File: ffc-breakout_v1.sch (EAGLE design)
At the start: 3 parts, among them X2 AMP_SFW16R-2STE1LF

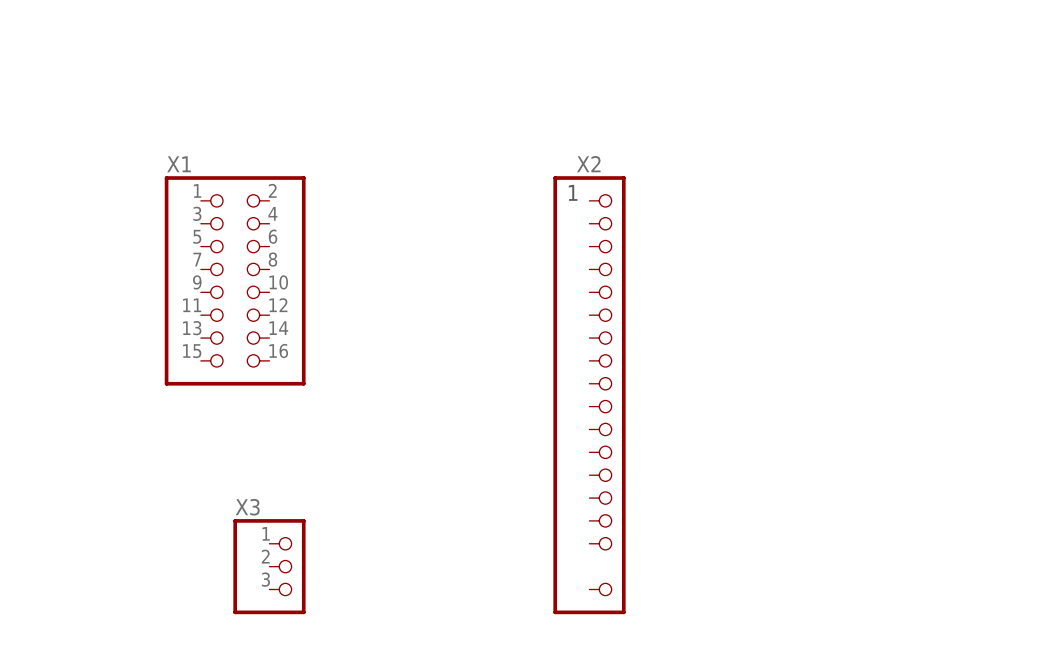
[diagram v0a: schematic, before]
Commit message: FFC breakout autoroute
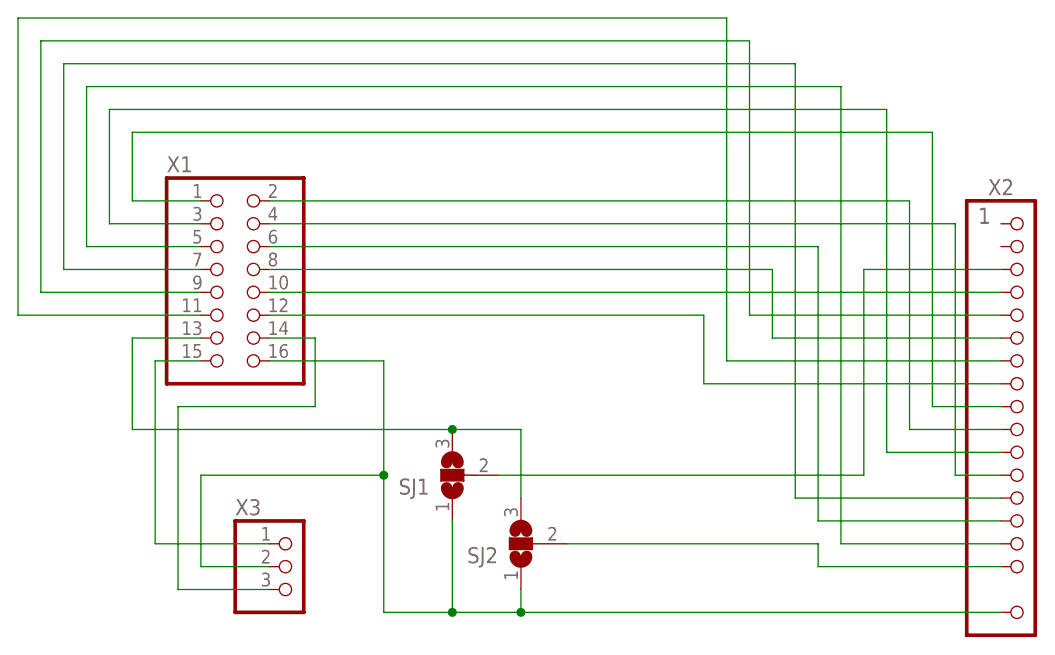
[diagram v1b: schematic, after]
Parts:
- added SJ1, SJ2: (no value), jumper:SJ2W
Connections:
- new net N$1: SJ1.1, SJ2.1, X1.16, X2.17, X3.2
- new net N$10: X1.4, X2.12
- new net N$11: X1.5, X2.15
- new net N$12: X1.6, X2.14
- new net N$13: X1.7, X2.13
- new net N$14: X1.8, X2.6
- new net N$15: X1.9, X2.5
- new net N$16: X1.10, X2.4
- new net N$17: X1.11, X2.7
- new net N$18: X1.12, X2.8
- new net N$2: X1.15, X3.1
- new net N$3: SJ1.3, SJ2.3, X1.13
- new net N$4: X1.14, X3.3
- new net N$5: SJ1.2, X2.3
- new net N$6: X1.1, X2.9
- new net N$7: SJ2.2, X2.16
- new net N$8: X1.2, X2.10
- new net N$9: X1.3, X2.11
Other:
- moved on the sheet: X2

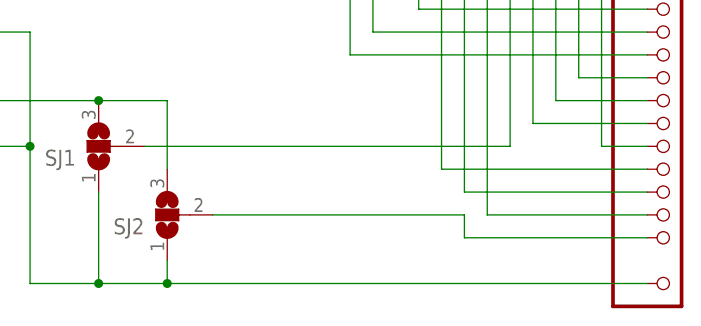
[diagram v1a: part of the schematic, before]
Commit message: FFC - much better autoroute + cleanup and markup
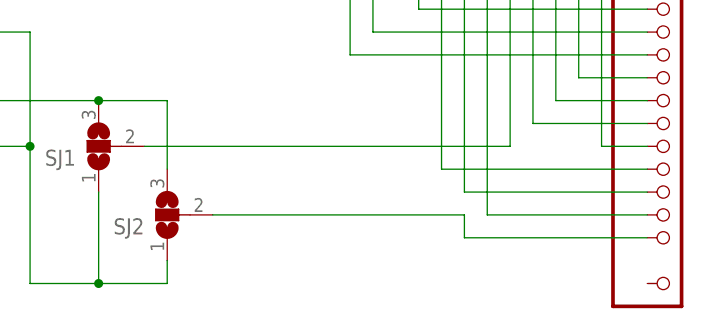
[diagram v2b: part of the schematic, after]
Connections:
- net N$1: no longer X2.17
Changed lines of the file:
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@@
 <classes>
 <class number="0" name="default" width="0.4064" drill="0.4064">
-<clearance class="0" value="0.127"/>
+<clearance class="0" value="0.2032"/>
 </class>
 </classes>
@@
 <wire x1="58.42" y1="45.72" x2="71.12" y2="45.72" width="0.1524" layer="91"/>
 <wire x1="71.12" y1="45.72" x2="71.12" y2="33.02" width="0.1524" layer="91"/>
-<pinref part="X2" gate="G$1" pin="17"/>
 <wire x1="71.12" y1="33.02" x2="71.12" y2="17.78" width="0.1524" layer="91"/>
 <wire x1="71.12" y1="17.78" x2="78.74" y2="17.78" width="0.1524" layer="91"/>
 <pinref part="X3" gate="A" pin="2"/>
 <wire x1="78.74" y1="17.78" x2="86.36" y2="17.78" width="0.1524" layer="91"/>
-<wire x1="86.36" y1="17.78" x2="139.7" y2="17.78" width="0.1524" layer="91"/>
 <wire x1="58.42" y1="22.86" x2="50.8" y2="22.86" width="0.1524" layer="91"/>
 <wire x1="50.8" y1="22.86" x2="50.8" y2="33.02" width="0.1524" layer="91"/>
@@
 <pinref part="SJ2" gate="G$1" pin="1"/>
 <wire x1="86.36" y1="20.32" x2="86.36" y2="17.78" width="0.1524" layer="91"/>
-<junction x="86.36" y="17.78"/>
 </segment>
 </net>
